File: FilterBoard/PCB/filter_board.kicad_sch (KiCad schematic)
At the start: 24 parts, among them J2 Banana Terminals

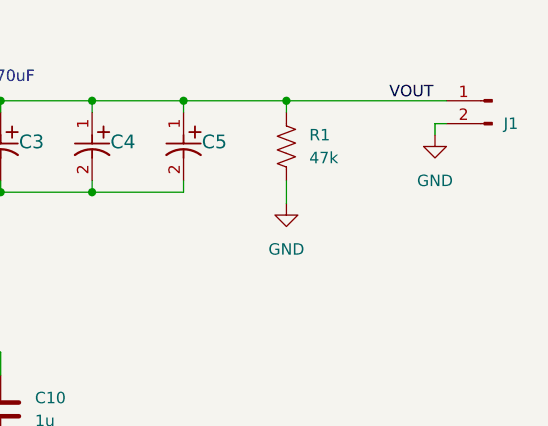
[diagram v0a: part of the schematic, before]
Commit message: Filter board layout tweaks
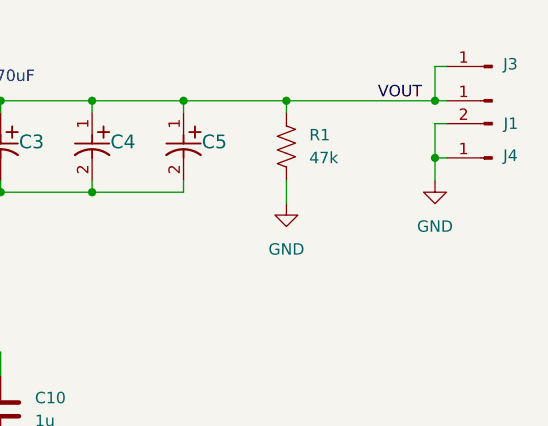
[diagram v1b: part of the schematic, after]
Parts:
- added J3, J4: Conn_01x01_Pin, FilterBoardLib:Wire_Pad, symbol Connector:Conn_01x01_Pin
- J1: footprint (none) -> FilterBoardLib:Banana_Terminals
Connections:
- net GND: now also J4.1 (Pin_1)
- net VOUT: now also J3.1 (Pin_1)
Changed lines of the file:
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@@
 	)
 	(junction
+		(at 220.98 87.63)
+		(diameter 0)
+		(color 0 0 0 0)
+	)
+	(junction
 		(at 146.05 115.57)
 		(diameter 0)
@@
 	)
 	(junction
+		(at 220.98 93.98)
+		(diameter 0)
+		(color 0 0 0 0)
+	)
+	(junction
 		(at 172.72 87.63)
 		(diameter 0)
@@
 	(wire
 		(pts
+			(xy 220.98 87.63) (xy 222.25 87.63)
+		)
+		(stroke
+			(width 0)
+			(type default)
+		)
+	)
+	(wire
+		(pts
 			(xy 152.4 97.79) (xy 152.4 100.33)
 		)
@@
 	(wire
 		(pts
-			(xy 204.47 87.63) (xy 222.25 87.63)
+			(xy 204.47 87.63) (xy 220.98 87.63)
 		)
 		(stroke
@@
 	(wire
 		(pts
+			(xy 220.98 83.82) (xy 220.98 87.63)
+		)
+		(stroke
+			(width 0)
+			(type default)
+		)
+	)
+	(wire
+		(pts
 			(xy 152.4 127) (xy 152.4 129.54)
 		)
@@
 	(wire
 		(pts
-			(xy 220.98 91.44) (xy 220.98 90.17)
+			(xy 220.98 96.52) (xy 220.98 93.98)
 		)
 		(stroke
@@
 	(wire
 		(pts
+			(xy 220.98 83.82) (xy 222.25 83.82)
+		)
+		(stroke
+			(width 0)
+			(type default)
+		)
+	)
+	(wire
+		(pts
 			(xy 57.15 87.63) (xy 69.85 87.63)
 		)
@@
 	(wire
 		(pts
+			(xy 220.98 90.17) (xy 220.98 93.98)
+		)
+		(stroke
+			(width 0)
+			(type default)
+		)
+	)
+	(wire
+		(pts
+			(xy 220.98 93.98) (xy 222.25 93.98)
+		)
+		(stroke
+			(width 0)
+			(type default)
+		)
+	)
+	(wire
+		(pts
 			(xy 87.63 127) (xy 87.63 129.54)
 		)
@@
 	)
 	(label "VOUT"
-		(at 215.9 87.63 0)
+		(at 214.63 87.63 0)
 		(fields_autoplaced yes)
 		(effects
@@
 	)
 	(symbol
+		(lib_id "Connector:Conn_01x01_Pin")
+		(at 227.33 83.82 180)
+		(unit 1)
+		(exclude_from_sim no)
+		(in_bom yes)
+		(on_board yes)
+		(dnp no)
+		(property "Reference" "J3"
+			(at 229.362 83.566 0)
+			(effects
+				(font
+					(size 1.27 1.27)
+				)
+			)
+		)
+		(property "Value" "Conn_01x01_Pin"
+			(at 226.695 81.28 0)
+			(effects
+				(font
+					(size 1.27 1.27)
+				)
+				(hide yes)
+			)
+		)
+		(property "Footprint" "FilterBoardLib:Wire_Pad"
+			(at 227.33 83.82 0)
+			(effects
+				(font
+					(size 1.27 1.27)
+				)
+				(hide yes)
+			)
+		)
+		(property "Datasheet" "~"
+			(at 227.33 83.82 0)
+			(effects
+				(font
+					(size 1.27 1.27)
+				)
+				(hide yes)
+			)
+		)
+		(property "Description" "Generic connector, single row, 01x01, script generated"
+			(at 227.33 83.82 0)
+			(effects
+				(font
+					(size 1.27 1.27)
+				)
+				(hide yes)
+			)
+		)
+		(pin "1"
+		)
+		(instances
+			(project ""
+				(path "/5a2b3a91-b284-4bf4-87fa-ab3b35aed5d3"
+					(reference "J3")
+					(unit 1)
+				)
+			)
+		)
+	)
+	(symbol
 		(lib_id "power:GND")
 		(at 152.4 154.94 0)
@@
 			)
 		)
-		(property "Footprint" ""
+		(property "Footprint" "FilterBoardLib:Banana_Terminals"
 			(at 227.33 87.63 0)
 			(effects
@@
 	(symbol
 		(lib_id "power:GND")
-		(at 220.98 91.44 0)
+		(at 220.98 96.52 0)
 		(unit 1)
 		(exclude_from_sim no)
@@
 		(fields_autoplaced yes)
 		(property "Reference" "#PWR03"
-			(at 220.98 97.79 0)
+			(at 220.98 102.87 0)
 			(effects
 				(font
@@
 		)
 		(property "Value" "GND"
-			(at 220.98 96.52 0)
+			(at 220.98 101.6 0)
 			(effects
 				(font
@@
 		)
 		(property "Footprint" ""
-			(at 220.98 91.44 0)
+			(at 220.98 96.52 0)
 			(effects
 				(font
@@
 		)
 		(property "Datasheet" ""
-			(at 220.98 91.44 0)
+			(at 220.98 96.52 0)
 			(effects
 				(font
@@
 		)
 		(property "Description" "Power symbol creates a global label with name \"GND\" , ground"
-			(at 220.98 91.44 0)
+			(at 220.98 96.52 0)
 			(effects
 				(font
@@
 					(unit 1)
 				)
+			)
+		)
+	)
+	(symbol
+		(lib_id "Connector:Conn_01x01_Pin")
+		(at 227.33 93.98 180)
+		(unit 1)
+		(exclude_from_sim no)
+		(in_bom yes)
+		(on_board yes)
+		(dnp no)
+		(property "Reference" "J4"
+			(at 229.362 93.726 0)
+			(effects
+				(font
+					(size 1.27 1.27)
+				)
+			)
+		)
+		(property "Value" "Conn_01x01_Pin"
+			(at 226.695 91.44 0)
+			(effects
+				(font
+					(size 1.27 1.27)
+				)
+				(hide yes)
+			)
+		)
+		(property "Footprint" "FilterBoardLib:Wire_Pad"
+			(at 227.33 93.98 0)
+			(effects
+				(font
+					(size 1.27 1.27)
+				)
+				(hide yes)
+			)
+		)
+		(property "Datasheet" "~"
+			(at 227.33 93.98 0)
+			(effects
+				(font
+					(size 1.27 1.27)
+				)
+				(hide yes)
+			)
+		)
+		(property "Description" "Generic connector, single row, 01x01, script generated"
+			(at 227.33 93.98 0)
+			(effects
+				(font
+					(size 1.27 1.27)
+				)
+				(hide yes)
+			)
+		)
+		(pin "1"
+		)
+		(instances
+			(project "filter_board"
+				(path "/5a2b3a91-b284-4bf4-87fa-ab3b35aed5d3"
+					(reference "J4")
+					(unit 1)
+				)
